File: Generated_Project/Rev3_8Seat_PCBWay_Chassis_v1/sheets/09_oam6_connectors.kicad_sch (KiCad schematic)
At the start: 0 parts

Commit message: Raise Rev3 chassis to 8 electrically designed seats.
Name v1.0 power/PE/clock nets on all eight OAM seats toward two DNP
PM8536B-FEI (x8 per GCD), keep SB175 star + local P48V pours, and generate
the 12-layer 2.0 mm stuffed-switch target. First stuffing may still populate
two modules; the PCB does not need a respin for the other six.

Do not fabricate. Do not energize P48V.

Co-authored-by: zivzancoeli-commits <zivzancoeli-commits@users.noreply.github.com>
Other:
- note added: "OAM6 connector instances — electrically designed; module may be DNP. Footprint: Molex 218910-1115 candidate (geometry). Hermaphroditic — mates with itself (Farnell 2189101115: Mates With 2189101115; mated height 5.00 mm). Pad nets assigned on the PCB from the v1.0 CSV for this seat: P48V/P12V1/P3V3/GND, PE (16 lanes) toward SW1 PM8536B-FEI DNP (seats 4-7), PE_REFCLK / PERST# / HOST_PWRGD (ENABLE)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"
- note removed: "OAM6 connector instances — MECHANICAL + POWER ONLY (populate later). Same 2x Molex 218910-1115 land pattern and Fig 2 M3.5 holes as seats 0-1. PCIe / xGMI / clock / mgmt pads have NO NET on this seat. needs on-board PCIe switch — MPN Unknown. Power pads share P48V / P12V1 / P12V2 / P3V3 / GND with the rest of the board. P48V still NO POUR, DO NOT ENERGIZE. PVREF is a module output — never drive."
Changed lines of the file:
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@@
 		(date "2026-08-21")
 		(rev "Rev3_8Seat_PCBWay_v1")
-		(comment 1 "DO NOT FABRICATE. DO NOT ENERGIZE P48V. Ticket 167157 open.")
-		(comment 2 "Documentation sheet — no invented nets")
-		(comment 3 "Pin names: OAM Pin map rev 1.0.xlsx — OCP generic, NOT AMD overlay")
-		(comment 4 "r2.0 maps UNUSABLE. P3V3=2 Conn0 C1/C2. 8-seat PCBWay chassis stub.")
+        (comment 1 "DO NOT FABRICATE. DO NOT ENERGIZE P48V. Molex 60V written 2026-08-18; 1.2A/contact OPEN.")
+        (comment 2 "Documentation sheet — no invented nets")
+        (comment 3 "Pin names: OAM Pin map rev 1.0.xlsx — OCP generic, NOT AMD overlay")
+        (comment 4 "r2.0 UNUSABLE. P3V3=Conn0 C1/C2. 12L 2.0mm stuffed-switch TARGET. Star-fed P48V.")
 	)
-	(text "OAM6 connector instances — MECHANICAL + POWER ONLY (populate later).\n\nSame 2x Molex 218910-1115 land pattern and Fig 2 M3.5 holes as seats 0-1.\nPCIe / xGMI / clock / mgmt pads have NO NET on this seat.\n\nneeds on-board PCIe switch — MPN Unknown.\n\nPower pads share P48V / P12V1 / P12V2 / P3V3 / GND with the rest of the board.\nP48V still NO POUR, DO NOT ENERGIZE. PVREF is a module output — never drive.\n"
+	(text "OAM6 connector instances — electrically designed; module may be DNP.\n\nFootprint: Molex 218910-1115 candidate (geometry). Hermaphroditic — mates with itself\n(Farnell 2189101115: Mates With 2189101115; mated height 5.00 mm).\n\nPad nets assigned on the PCB from the v1.0 CSV for this seat:\nP48V/P12V1/P3V3/GND, PE (16 lanes) toward SW1 PM8536B-FEI DNP (seats 4-7),\nPE_REFCLK / PERST# / HOST_PWRGD (ENABLE). S1-S7 have NO NET (no xGMI).\nTEST*/RFU/DO_NOT_USE unmapped. PVREF is a module output — never drive.\nP12V2 named from v1.0 but Unknown / may be NC. P48V is a LOCAL pour after a ~15 A fuse keepout.\n\nMODULE_ID / LINK_CONFIG 1k pulldowns NOT placed (AMD overlay unknown).\n"
 		(exclude_from_sim no)
 		(at 20.32 20.32 0)
@@
 		(effects (font (size 1.27 1.27)) (justify left))
 	)
+	(hierarchical_label "OAM6_PE_REFCLKP"
+		(shape bidirectional)
+		(at 25.4 180.48000000000008 0)
+		(effects (font (size 1.27 1.27)) (justify left))
+	)
+	(hierarchical_label "OAM6_PE_REFCLKN"
+		(shape bidirectional)
+		(at 25.4 185.5600000000001 0)
+		(effects (font (size 1.27 1.27)) (justify left))
+	)
+	(hierarchical_label "OAM6_PERST#"
+		(shape bidirectional)
+		(at 25.4 190.6400000000001 0)
+		(effects (font (size 1.27 1.27)) (justify left))
+	)
+	(hierarchical_label "OAM6_HOST_PWRGD"
+		(shape bidirectional)
+		(at 25.4 195.7200000000001 0)
+		(effects (font (size 1.27 1.27)) (justify left))
+	)
+	(hierarchical_label "OAM6_MODULE_PWRGD"
+		(shape bidirectional)
+		(at 25.4 200.80000000000013 0)
+		(effects (font (size 1.27 1.27)) (justify left))
+	)
+	(hierarchical_label "OAM6_WARMRST#"
+		(shape bidirectional)
+		(at 25.4 205.88000000000014 0)
+		(effects (font (size 1.27 1.27)) (justify left))
+	)
+	(hierarchical_label "OAM6_PWRBRK#"
+		(shape bidirectional)
+		(at 25.4 210.96000000000015 0)
+		(effects (font (size 1.27 1.27)) (justify left))
+	)
+	(hierarchical_label "OAM6_PRSNT0#"
+		(shape bidirectional)
+		(at 25.4 216.04000000000016 0)
+		(effects (font (size 1.27 1.27)) (justify left))
+	)
+	(hierarchical_label "OAM6_SMBus_SLV_D"
+		(shape bidirectional)
+		(at 25.4 221.12000000000018 0)
+		(effects (font (size 1.27 1.27)) (justify left))
+	)
+	(hierarchical_label "OAM6_SMBus_SLV_CLK"
+		(shape bidirectional)
+		(at 25.4 226.2000000000002 0)
+		(effects (font (size 1.27 1.27)) (justify left))
+	)

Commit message: Label PEX8780-AB80BI G as the only switch CANDIDATE (DNP).
Keepout is one 35 mm 1156-FCBGA for 8x x8 Gen3 plus one x16 host uplink.
Do not invent a second MPN. Do not stuff. 8-layer is likely if this BGA
is ever assembled; PCBWay 1156-FCBGA attach remains Unknown.

Still do not fabricate or energize P48V. No xGMI, no CEM.

Co-authored-by: zivzancoeli-commits <zivzancoeli-commits@users.noreply.github.com>
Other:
- note added: "OAM6 connector instances — electrically designed; module may be DNP. Footprint: Molex 218910-1115 candidate (geometry). Hermaphroditic — mates with itself (Farnell 2189101115: Mates With 2189101115; mated height 5.00 mm). Pad nets assigned on the PCB from the v1.0 CSV for this seat: P48V/P12V1/P3V3/GND, PE (16 lanes) toward PEX8780-AB80BI G CANDIDATE DNP (8x x8 + one x16 uplink; not stuffed), PE_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"
- note removed: "OAM6 connector instances — electrically designed; module may be DNP. Footprint: Molex 218910-1115 candidate (geometry). Hermaphroditic — mates with itself (Farnell 2189101115: Mates With 2189101115; mated height 5.00 mm). Pad nets assigned on the PCB from the v1.0 CSV for this seat: P48V/P12V1/P3V3/GND, PE (16 lanes) toward SW1 PM8536B-FEI DNP (seats 4-7), PE_REFCLK / PERST# / HOST_PWRGD (ENABLE)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"
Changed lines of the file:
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@@
         (comment 4 "r2.0 UNUSABLE. P3V3=Conn0 C1/C2. 12L 2.0mm stuffed-switch TARGET. Star-fed P48V.")
 	)
-	(text "OAM6 connector instances — electrically designed; module may be DNP.\n\nFootprint: Molex 218910-1115 candidate (geometry). Hermaphroditic — mates with itself\n(Farnell 2189101115: Mates With 2189101115; mated height 5.00 mm).\n\nPad nets assigned on the PCB from the v1.0 CSV for this seat:\nP48V/P12V1/P3V3/GND, PE (16 lanes) toward SW1 PM8536B-FEI DNP (seats 4-7),\nPE_REFCLK / PERST# / HOST_PWRGD (ENABLE). S1-S7 have NO NET (no xGMI).\nTEST*/RFU/DO_NOT_USE unmapped. PVREF is a module output — never drive.\nP12V2 named from v1.0 but Unknown / may be NC. P48V is a LOCAL pour after a ~15 A fuse keepout.\n\nMODULE_ID / LINK_CONFIG 1k pulldowns NOT placed (AMD overlay unknown).\n"
+	(text "OAM6 connector instances — electrically designed; module may be DNP.\n\nFootprint: Molex 218910-1115 candidate (geometry). Hermaphroditic — mates with itself\n(Farnell 2189101115: Mates With 2189101115; mated height 5.00 mm).\n\nPad nets assigned on the PCB from the v1.0 CSV for this seat:\nP48V/P12V1/P3V3/GND, PE (16 lanes) toward PEX8780-AB80BI G CANDIDATE DNP (8x x8 + one x16 uplink; not stuffed),\nPE_REFCLK / PERST# / HOST_PWRGD (ENABLE). S1-S7 have NO NET (no xGMI).\nTEST*/RFU/DO_NOT_USE unmapped. PVREF is a module output — never drive.\nP12V2 named from v1.0 but Unknown / may be NC. P48V is a LOCAL pour after a ~15 A fuse keepout.\n\nMODULE_ID / LINK_CONFIG 1k pulldowns NOT placed (AMD overlay unknown).\n"
 		(exclude_from_sim no)
 		(at 20.32 20.32 0)

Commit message: Make PM8536B-FEI the PRIMARY switch keepout (DNP x2).
Two 37.5 mm 1311-FCBGA courtyards, x8 per GCD (SW0 seats 0-3, SW1 4-7),
two CPU x16 uplinks. PEX8780 stays a cheaper 80-lane alt in docs only.
GCD1 = SERDES_7 remains Inferred. No CEM, no xGMI, do not fabricate.

Co-authored-by: zivzancoeli-commits <zivzancoeli-commits@users.noreply.github.com>
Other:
- note added: "OAM6 connector instances — electrically designed; module may be DNP. Footprint: Molex 218910-1115 candidate (geometry). Hermaphroditic — mates with itself (Farnell 2189101115: Mates With 2189101115; mated height 5.00 mm). Pad nets assigned on the PCB from the v1.0 CSV for this seat: P48V/P12V1/P3V3/GND, PE (16 lanes) toward SW1 PM8536B-FEI DNP PRIMARY (seats 4-7, x8/GCD), PE_REFCLK / PERST# / HOS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"
- note removed: "OAM6 connector instances — electrically designed; module may be DNP. Footprint: Molex 218910-1115 candidate (geometry). Hermaphroditic — mates with itself (Farnell 2189101115: Mates With 2189101115; mated height 5.00 mm). Pad nets assigned on the PCB from the v1.0 CSV for this seat: P48V/P12V1/P3V3/GND, PE (16 lanes) toward PEX8780-AB80BI G CANDIDATE DNP (8x x8 + one x16 uplink; not stuffed), PE_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"
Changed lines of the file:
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@@
         (comment 2 "Documentation sheet — no invented nets")
         (comment 3 "Pin names: OAM Pin map rev 1.0.xlsx — OCP generic, NOT AMD overlay")
-        (comment 4 "r2.0 UNUSABLE. P3V3=Conn0 C1/C2. 12L 2.0mm stuffed-switch TARGET. Star-fed P48V.")
+        (comment 4 "r2.0 UNUSABLE. P3V3=Conn0 C1/C2. 12L 2.0mm stuffed-switch TARGET. 2x PM8536 DNP. Star-fed P48V.")
 	)
-	(text "OAM6 connector instances — electrically designed; module may be DNP.\n\nFootprint: Molex 218910-1115 candidate (geometry). Hermaphroditic — mates with itself\n(Farnell 2189101115: Mates With 2189101115; mated height 5.00 mm).\n\nPad nets assigned on the PCB from the v1.0 CSV for this seat:\nP48V/P12V1/P3V3/GND, PE (16 lanes) toward PEX8780-AB80BI G CANDIDATE DNP (8x x8 + one x16 uplink; not stuffed),\nPE_REFCLK / PERST# / HOST_PWRGD (ENABLE). S1-S7 have NO NET (no xGMI).\nTEST*/RFU/DO_NOT_USE unmapped. PVREF is a module output — never drive.\nP12V2 named from v1.0 but Unknown / may be NC. P48V is a LOCAL pour after a ~15 A fuse keepout.\n\nMODULE_ID / LINK_CONFIG 1k pulldowns NOT placed (AMD overlay unknown).\n"
+	(text "OAM6 connector instances — electrically designed; module may be DNP.\n\nFootprint: Molex 218910-1115 candidate (geometry). Hermaphroditic — mates with itself\n(Farnell 2189101115: Mates With 2189101115; mated height 5.00 mm).\n\nPad nets assigned on the PCB from the v1.0 CSV for this seat:\nP48V/P12V1/P3V3/GND, PE (16 lanes) toward SW1 PM8536B-FEI DNP PRIMARY (seats 4-7, x8/GCD),\nPE_REFCLK / PERST# / HOST_PWRGD (ENABLE). S1-S7 have NO NET (no xGMI).\nTEST*/RFU/DO_NOT_USE unmapped. PVREF is a module output — never drive.\nP12V2 named from v1.0 but Unknown / may be NC. P48V is a LOCAL pour after a ~15 A fuse keepout.\n\nMODULE_ID / LINK_CONFIG 1k pulldowns NOT placed (AMD overlay unknown).\n"
 		(exclude_from_sim no)
 		(at 20.32 20.32 0)

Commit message: Make the Rev3 8-seat chassis full-width capable with four PM8536 DNP courtyards.
Same 492x372 POWER+MECH PCB; architecture is now 16 named x16 PE buses
(PE_Sn_GCD0_x16 + PE_Sn_GCD1_x16) and SW0-SW3 keepouts. Two 96-lane
switches are enough for 8x x8/GCD, not 8x x16/GCD. Host stays X11DPH-T
(~80 lanes) and cannot light 256 downstream. Do not energize P48V.

Co-authored-by: zivzancoeli-commits <zivzancoeli-commits@users.noreply.github.com>
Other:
- note added: "OAM6 connector instances — EIGHT-SEAT STUFF (populate path 8; stuff SW2/SW3 later; no respin). Footprint: Molex 218910-1115 candidate (geometry). Hermaphroditic — mates with itself (Farnell 2189101115: Mates With 2189101115; mated height 5.00 mm). Pad nets assigned on the PCB from the v1.0 CSV for this seat: P48V/P12V1/P3V3/GND, Conn0 PE 16 lanes (PE_S6_GCD0_x16) toward SW3 PM8536B-FEI DNP (seats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"
- note removed: "OAM6 connector instances — electrically designed; module may be DNP. Footprint: Molex 218910-1115 candidate (geometry). Hermaphroditic — mates with itself (Farnell 2189101115: Mates With 2189101115; mated height 5.00 mm). Pad nets assigned on the PCB from the v1.0 CSV for this seat: P48V/P12V1/P3V3/GND, PE (16 lanes) toward SW1 PM8536B-FEI DNP PRIMARY (seats 4-7, x8/GCD), PE_REFCLK / PERST# / HOS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"
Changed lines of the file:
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@@
         (comment 2 "Documentation sheet — no invented nets")
         (comment 3 "Pin names: OAM Pin map rev 1.0.xlsx — OCP generic, NOT AMD overlay")
-        (comment 4 "r2.0 UNUSABLE. P3V3=Conn0 C1/C2. 12L 2.0mm stuffed-switch TARGET. 2x PM8536 DNP. Star-fed P48V.")
+        (comment 4 "r2.0 UNUSABLE. P3V3=Conn0 C1/C2. 12L 2.0mm stuffed-switch TARGET. 4x PM8536 DNP. Star-fed P48V.")
 	)
-	(text "OAM6 connector instances — electrically designed; module may be DNP.\n\nFootprint: Molex 218910-1115 candidate (geometry). Hermaphroditic — mates with itself\n(Farnell 2189101115: Mates With 2189101115; mated height 5.00 mm).\n\nPad nets assigned on the PCB from the v1.0 CSV for this seat:\nP48V/P12V1/P3V3/GND, PE (16 lanes) toward SW1 PM8536B-FEI DNP PRIMARY (seats 4-7, x8/GCD),\nPE_REFCLK / PERST# / HOST_PWRGD (ENABLE). S1-S7 have NO NET (no xGMI).\nTEST*/RFU/DO_NOT_USE unmapped. PVREF is a module output — never drive.\nP12V2 named from v1.0 but Unknown / may be NC. P48V is a LOCAL pour after a ~15 A fuse keepout.\n\nMODULE_ID / LINK_CONFIG 1k pulldowns NOT placed (AMD overlay unknown).\n"
+	(text "OAM6 connector instances — EIGHT-SEAT STUFF (populate path 8; stuff SW2/SW3 later; no respin).\n\nFootprint: Molex 218910-1115 candidate (geometry). Hermaphroditic — mates with itself\n(Farnell 2189101115: Mates With 2189101115; mated height 5.00 mm).\n\nPad nets assigned on the PCB from the v1.0 CSV for this seat:\nP48V/P12V1/P3V3/GND, Conn0 PE 16 lanes (PE_S6_GCD0_x16) toward SW3 PM8536B-FEI DNP\n(seats 6,7, 16 US + 64 DS hypothesis — not a ball map),\nPE_S6_GCD1_x16 named-only (pins Unknown; not S1-S7),\nPE_REFCLK / PERST# / HOST_PWRGD (ENABLE). S1-S7 have NO NET (no xGMI).\nTEST*/RFU/DO_NOT_USE unmapped. PVREF is a module output — never drive.\nP12V2 named from v1.0 but Unknown / may be NC. P48V is a LOCAL pour after a ~15 A fuse keepout.\n\nMODULE_ID / LINK_CONFIG 1k pulldowns NOT placed (AMD overlay unknown).\n"
 		(exclude_from_sim no)
 		(at 20.32 20.32 0)
@@
 		(effects (font (size 1.27 1.27)) (justify left))
 	)
+	(hierarchical_label "PE_S6_GCD0_x16"
+		(shape bidirectional)
+		(at 25.4 231.2800000000002 0)
+		(effects (font (size 1.27 1.27)) (justify left))
+	)
+	(hierarchical_label "PE_S6_GCD1_x16"
+		(shape bidirectional)
+		(at 25.4 236.3600000000002 0)
+		(effects (font (size 1.27 1.27)) (justify left))
+	)

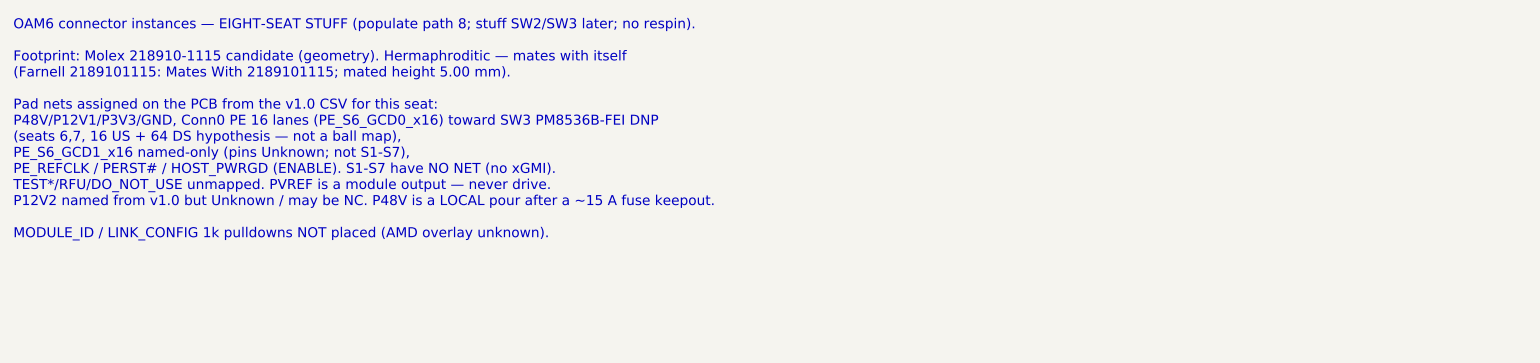
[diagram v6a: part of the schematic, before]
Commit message: Retarget Rev3 first article to seats 0-1 GCD0 x16 (2-module path).
Same 8-seat PCB. Without overlay, 2x MI250X means two modules can sit
and at most GCD0 on each can be named toward the host keepout (2 GCDs),
not 2x full-width (4 GCDs). Conn0 OCP PCIE_* is the only legal host PE.
No CEM/MCIO MPN. Do not energize P48V.

Co-authored-by: zivzancoeli-commits <zivzancoeli-commits@users.noreply.github.com>
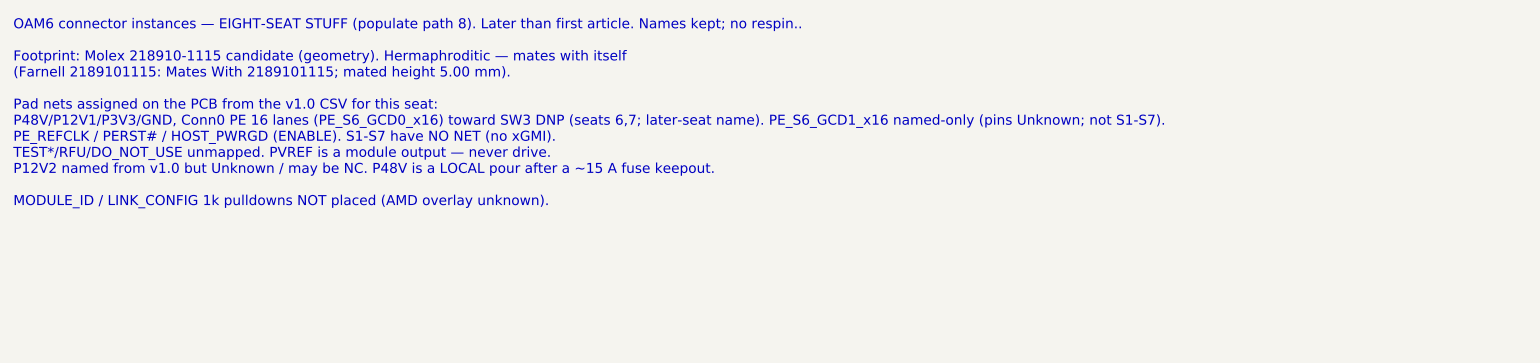
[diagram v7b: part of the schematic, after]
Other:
- note added: "OAM6 connector instances — EIGHT-SEAT STUFF (populate path 8). Later than first article. Names kept; no respin.. Footprint: Molex 218910-1115 candidate (geometry). Hermaphroditic — mates with itself (Farnell 2189101115: Mates With 2189101115; mated height 5.00 mm). Pad nets assigned on the PCB from the v1.0 CSV for this seat: P48V/P12V1/P3V3/GND, Conn0 PE 16 lanes (PE_S6_GCD0_x16) toward SW3 DNP 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"
- note removed: "OAM6 connector instances — EIGHT-SEAT STUFF (populate path 8; stuff SW2/SW3 later; no respin). Footprint: Molex 218910-1115 candidate (geometry). Hermaphroditic — mates with itself (Farnell 2189101115: Mates With 2189101115; mated height 5.00 mm). Pad nets assigned on the PCB from the v1.0 CSV for this seat: P48V/P12V1/P3V3/GND, Conn0 PE 16 lanes (PE_S6_GCD0_x16) toward SW3 PM8536B-FEI DNP (seats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"
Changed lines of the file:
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@@
         (comment 4 "r2.0 UNUSABLE. P3V3=Conn0 C1/C2. 12L 2.0mm stuffed-switch TARGET. 4x PM8536 DNP. Star-fed P48V.")
 	)
-	(text "OAM6 connector instances — EIGHT-SEAT STUFF (populate path 8; stuff SW2/SW3 later; no respin).\n\nFootprint: Molex 218910-1115 candidate (geometry). Hermaphroditic — mates with itself\n(Farnell 2189101115: Mates With 2189101115; mated height 5.00 mm).\n\nPad nets assigned on the PCB from the v1.0 CSV for this seat:\nP48V/P12V1/P3V3/GND, Conn0 PE 16 lanes (PE_S6_GCD0_x16) toward SW3 PM8536B-FEI DNP\n(seats 6,7, 16 US + 64 DS hypothesis — not a ball map),\nPE_S6_GCD1_x16 named-only (pins Unknown; not S1-S7),\nPE_REFCLK / PERST# / HOST_PWRGD (ENABLE). S1-S7 have NO NET (no xGMI).\nTEST*/RFU/DO_NOT_USE unmapped. PVREF is a module output — never drive.\nP12V2 named from v1.0 but Unknown / may be NC. P48V is a LOCAL pour after a ~15 A fuse keepout.\n\nMODULE_ID / LINK_CONFIG 1k pulldowns NOT placed (AMD overlay unknown).\n"
+	(text "OAM6 connector instances — EIGHT-SEAT STUFF (populate path 8). Later than first article. Names kept; no respin..\n\nFootprint: Molex 218910-1115 candidate (geometry). Hermaphroditic — mates with itself\n(Farnell 2189101115: Mates With 2189101115; mated height 5.00 mm).\n\nPad nets assigned on the PCB from the v1.0 CSV for this seat:\nP48V/P12V1/P3V3/GND, Conn0 PE 16 lanes (PE_S6_GCD0_x16) toward SW3 DNP (seats 6,7; later-seat name). PE_S6_GCD1_x16 named-only (pins Unknown; not S1-S7).\nPE_REFCLK / PERST# / HOST_PWRGD (ENABLE). S1-S7 have NO NET (no xGMI).\nTEST*/RFU/DO_NOT_USE unmapped. PVREF is a module output — never drive.\nP12V2 named from v1.0 but Unknown / may be NC. P48V is a LOCAL pour after a ~15 A fuse keepout.\n\nMODULE_ID / LINK_CONFIG 1k pulldowns NOT placed (AMD overlay unknown).\n"
 		(exclude_from_sim no)
 		(at 20.32 20.32 0)
